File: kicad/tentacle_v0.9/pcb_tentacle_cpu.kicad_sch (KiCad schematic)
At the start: 27 parts, among them J201 Conn_02x05, U201 RP2040, U203 W25Q32JVS, X201 Oscillator-12MHz

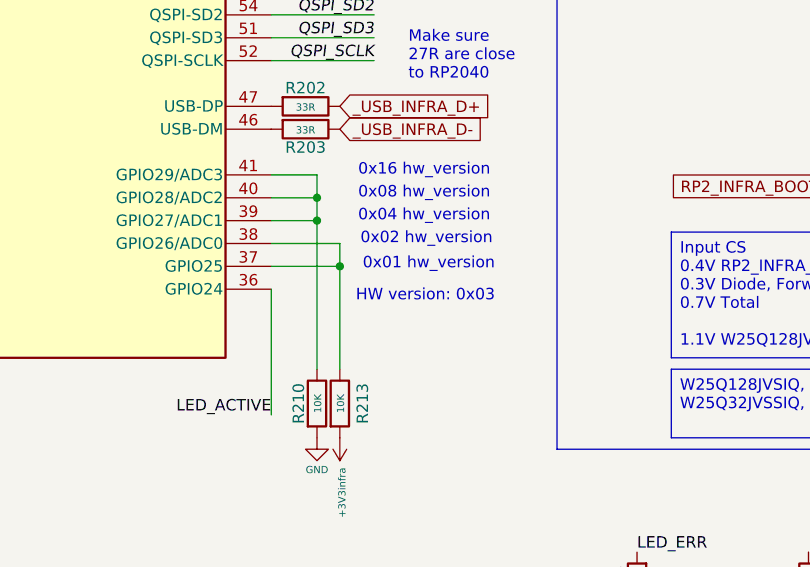
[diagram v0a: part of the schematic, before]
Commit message: Tentacle: v0.9.0: hw_version 0x03 -> 0x04
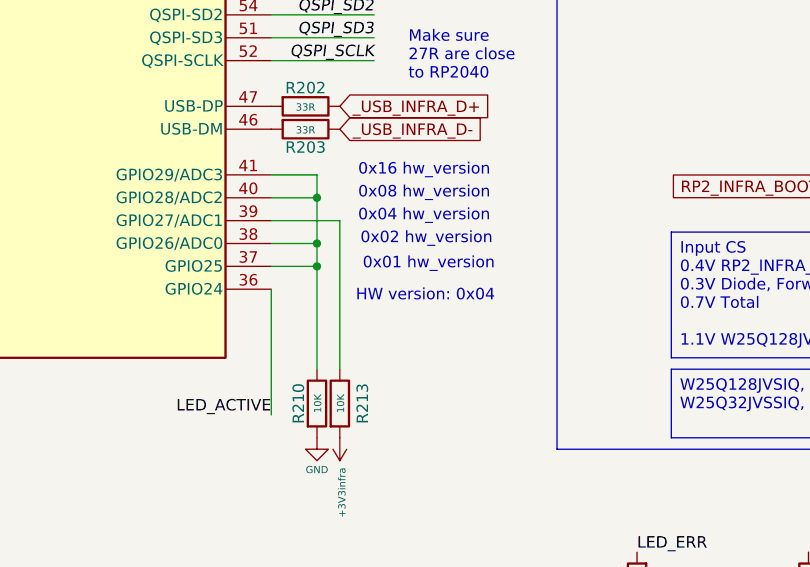
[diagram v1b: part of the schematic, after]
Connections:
- net at U201.37 (GPIO25), U201.38 (GPIO26/ADC0): now also R210.1, U201.40 (GPIO28/ADC2), U201.41 (GPIO29/ADC3); no longer R213.1
- new net: R213.1, U201.39 (GPIO27/ADC1)
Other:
- note added: "HW version: 0x04"
- note removed: "HW version: 0x03"
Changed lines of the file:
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@@
 		)
 	)
-	(text "HW version: 0x03"
+	(text "HW version: 0x04"
 		(exclude_from_sim no)
 		(at 133.858 108.204 0)
@@
 	)
 	(junction
-		(at 132.08 104.14)
-		(diameter 0)
-		(color 0 0 0 0)
-	)
-	(junction
 		(at 129.54 96.52)
 		(diameter 0)
@@
 	)
 	(junction
+		(at 129.54 101.6)
+		(diameter 0)
+		(color 0 0 0 0)
+	)
+	(junction
 		(at 107.95 30.48)
 		(diameter 1.016)
@@
 	)
 	(junction
-		(at 129.54 99.06)
+		(at 173.99 41.91)
+		(diameter 1.016)
+		(color 0 0 0 0)
+	)
+	(junction
+		(at 90.17 30.48)
+		(diameter 1.016)
+		(color 0 0 0 0)
+	)
+	(junction
+		(at 214.63 31.75)
+		(diameter 1.016)
+		(color 0 0 0 0)
+	)
+	(junction
+		(at 194.31 31.75)
+		(diameter 1.016)
+		(color 0 0 0 0)
+	)
+	(junction
+		(at 271.78 41.91)
+		(diameter 1.016)
+		(color 0 0 0 0)
+	)
+	(junction
+		(at 105.41 30.48)
+		(diameter 1.016)
+		(color 0 0 0 0)
+	)
+	(junction
+		(at 95.25 30.48)
+		(diameter 1.016)
+		(color 0 0 0 0)
+	)
+	(junction
+		(at 129.54 104.14)
 		(diameter 0)
-		(color 0 0 0 0)
-	)
-	(junction
-		(at 173.99 41.91)
-		(diameter 1.016)
-		(color 0 0 0 0)
-	)
-	(junction
-		(at 90.17 30.48)
-		(diameter 1.016)
-		(color 0 0 0 0)
-	)
-	(junction
-		(at 214.63 31.75)
-		(diameter 1.016)
-		(color 0 0 0 0)
-	)
-	(junction
-		(at 194.31 31.75)
-		(diameter 1.016)
-		(color 0 0 0 0)
-	)
-	(junction
-		(at 271.78 41.91)
-		(diameter 1.016)
-		(color 0 0 0 0)
-	)
-	(junction
-		(at 105.41 30.48)
-		(diameter 1.016)
-		(color 0 0 0 0)
-	)
-	(junction
-		(at 95.25 30.48)
-		(diameter 1.016)
 		(color 0 0 0 0)
 	)
@@
 	(wire
 		(pts
-			(xy 124.46 104.14) (xy 132.08 104.14)
-		)
-		(stroke
-			(width 0)
-			(type default)
-		)
-	)
-	(wire
-		(pts
 			(xy 44.45 48.26) (xy 53.34 48.26)
 		)
@@
 	(wire
 		(pts
-			(xy 132.08 101.6) (xy 132.08 104.14)
-		)
-		(stroke
-			(width 0)
-			(type default)
-		)
-	)
-	(wire
-		(pts
 			(xy 229.87 95.25) (xy 252.73 95.25)
 		)
@@
 	(wire
 		(pts
+			(xy 129.54 101.6) (xy 129.54 104.14)
+		)
+		(stroke
+			(width 0)
+			(type default)
+		)
+	)
+	(wire
+		(pts
 			(xy 124.46 96.52) (xy 129.54 96.52)
 		)
@@
 	(wire
 		(pts
-			(xy 124.46 101.6) (xy 132.08 101.6)
-		)
-		(stroke
-			(width 0)
-			(type default)
-		)
-	)
-	(wire
-		(pts
 			(xy 45.72 101.6) (xy 45.72 115.57)
 		)
@@
 	(wire
 		(pts
+			(xy 129.54 104.14) (xy 129.54 115.57)
+		)
+		(stroke
+			(width 0)
+			(type default)
+		)
+	)
+	(wire
+		(pts
 			(xy 124.46 93.98) (xy 129.54 93.98)
 		)
@@
 	(wire
 		(pts
+			(xy 124.46 101.6) (xy 129.54 101.6)
+		)
+		(stroke
+			(width 0)
+			(type default)
+		)
+	)
+	(wire
+		(pts
 			(xy 237.49 41.91) (xy 226.06 41.91)
 		)
@@
 	(wire
 		(pts
-			(xy 129.54 99.06) (xy 129.54 115.57)
-		)
-		(stroke
-			(width 0)
-			(type default)
-		)
-	)
-	(wire
-		(pts
 			(xy 237.49 31.75) (xy 248.92 31.75)
 		)
@@
 	(wire
 		(pts
+			(xy 124.46 99.06) (xy 132.08 99.06)
+		)
+		(stroke
+			(width 0)
+			(type default)
+		)
+	)
+	(wire
+		(pts
 			(xy 52.07 99.06) (xy 53.34 99.06)
 		)
@@
 		)
 	)
+	(wire
+		(pts
+			(xy 124.46 104.14) (xy 129.54 104.14)
+		)
+		(stroke
+			(width 0)
+			(type default)
+		)
+	)
 	(polyline
 		(pts
@@
 	(wire
 		(pts
-			(xy 124.46 99.06) (xy 129.54 99.06)
-		)
-		(stroke
-			(width 0)
-			(type default)
-		)
-	)
-	(wire
-		(pts
 			(xy 260.35 41.91) (xy 271.78 41.91)
 		)
@@
 	(wire
 		(pts
-			(xy 129.54 96.52) (xy 129.54 99.06)
+			(xy 129.54 96.52) (xy 129.54 101.6)
 		)
 		(stroke
@@
 	(wire
 		(pts
-			(xy 132.08 104.14) (xy 132.08 115.57)
-		)
-		(stroke
+			(xy 132.08 99.06) (xy 132.08 115.57)
+		)
+		(stroke
